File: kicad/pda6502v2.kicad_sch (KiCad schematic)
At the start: 87 parts

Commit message: kicad: schematic format version 20211123->20230121 (KiCad 7.0)
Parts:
- C1, C10, C11, C14, C15, C16, C17, C2, C22, C23, C24, C25, C26, C27, C3, C32, C4, C5, C6, C7, C8, C9: value (none) -> 0.1μF; footprint (none) -> Capacitor_SMD:C_0805_2012Metric_Pad1.18x1.45mm_HandSolder
- C12: value (none) -> 100uF; footprint (none) -> Capacitor_THT:CP_Radial_D5.0mm_P2.00mm
- C13: value (none) -> 10uF; footprint (none) -> Capacitor_THT:CP_Radial_D5.0mm_P2.00mm
- C18, C19: value (none) -> 10nF; footprint (none) -> Capacitor_SMD:C_0805_2012Metric_Pad1.18x1.45mm_HandSolder
- C20, C21: value (none) -> 10uF; footprint (none) -> Capacitor_SMD:C_0805_2012Metric_Pad1.18x1.45mm_HandSolder
- C28, C31: value (none) -> 1800 pf; footprint (none) -> Capacitor_SMD:C_0805_2012Metric_Pad1.18x1.45mm_HandSolder
- C29, C30: value (none) -> 10uF; footprint (none) -> Capacitor_Tantalum_SMD:CP_EIA-3528-15_AVX-H_Pad1.50x2.35mm_HandSolder
- D1: value (none) -> 1N5819; footprint (none) -> Diode_THT:D_DO-41_SOD81_P10.16mm_Horizontal
- D10, D3, D4, D5, D6, D7, D8, D9: value (none) -> LED; footprint (none) -> LED_SMD:LED_0805_2012Metric_Pad1.15x1.40mm_HandSolder
- D11: value (none) -> 1N4148W; footprint (none) -> Diode_SMD:D_SOD-123
- D2: value (none) -> LED; footprint (none) -> LED_THT:LED_D3.0mm
- J1: value (none) -> GPIO1; footprint (none) -> Connector_PinHeader_2.54mm:PinHeader_2x12_P2.54mm_Vertical
- J2: value (none) -> GPIO2; footprint (none) -> Connector_PinHeader_2.54mm:PinHeader_2x12_P2.54mm_Vertical
- J3: value (none) -> UART; footprint (none) -> Connector_PinHeader_2.54mm:PinHeader_2x06_P2.54mm_Vertical
- J4: value (none) -> Screw_Terminal_01x02; footprint (none) -> TerminalBlock_Phoenix:TerminalBlock_Phoenix_MPT-0,5-2-2.54_1x02_P2.54mm_Horizontal
- J5: value (none) -> Conn_02x04_Odd_Even; footprint (none) -> Connector_PinHeader_2.54mm:PinHeader_2x04_P2.54mm_Vertical
- J6: value (none) -> ICSP; footprint (none) -> Connector_PinHeader_2.54mm:PinHeader_2x03_P2.54mm_Vertical
- J7: value (none) -> SPI; footprint (none) -> Connector_PinHeader_2.54mm:PinHeader_2x10_P2.54mm_Vertical
- J8: value (none) -> FPGA_EXT; footprint (none) -> Connector_PinHeader_2.54mm:PinHeader_2x08_P2.54mm_Vertical
- J9: value (none) -> SID; footprint (none) -> Connector_PinHeader_2.54mm:PinHeader_2x04_P2.54mm_Vertical
- R1, R2, R21, R22, R23, R3, R4: value (none) -> 10K; footprint (none) -> Resistor_SMD:R_0805_2012Metric_Pad1.20x1.40mm_HandSolder
- R24: value (none) -> 255k; footprint (none) -> Resistor_SMD:R_0805_2012Metric_Pad1.20x1.40mm_HandSolder
- R25: value (none) -> 243k; footprint (none) -> Resistor_SMD:R_0805_2012Metric_Pad1.20x1.40mm_HandSolder
- R26: value (none) -> 0; footprint (none) -> Resistor_SMD:R_0805_2012Metric_Pad1.20x1.40mm_HandSolder
- R27: value (none) -> open; footprint (none) -> Resistor_SMD:R_0805_2012Metric_Pad1.20x1.40mm_HandSolder
- R28: value (none) -> 1K; footprint (none) -> Resistor_SMD:R_0805_2012Metric_Pad1.20x1.40mm_HandSolder
- R29, R30, R31, R32, R33, R34, R35, R36: value (none) -> 330; footprint (none) -> Resistor_SMD:R_0805_2012Metric_Pad1.20x1.40mm_HandSolder
- SW1: value (none) -> SW_Push; footprint (none) -> Button_Switch_THT:SW_PUSH_6mm_H5mm
- SW2: value (none) -> SW_Push; footprint (none) -> Connector_PinHeader_2.54mm:PinHeader_1x02_P2.54mm_Vertical
- U1: value (none) -> W65C02SxP; footprint (none) -> Package_DIP:DIP-40_W15.24mm
- U10: value (none) -> LT3030; footprint (none) -> Package_SO:HTSSOP-20-1EP_4.4x6.5mm_P0.65mm_EP2.85x4mm
- U11: value (none) -> SC28L92A1B; footprint (none) -> Package_QFP:PQFP-44_10x10mm_P0.8mm
- U2, U3: value (none) -> W65C22SxP; footprint (none) -> Package_DIP:DIP-40_W15.24mm
- U4: value (none) -> DS1818; footprint (none) -> Package_TO_SOT_SMD:SOT-23_Handsoldering
- U5: value (none) -> AS6C4008-55PCN; footprint (none) -> Package_DIP:DIP-32_W15.24mm
- U6: value (none) -> ARMSID; footprint (none) -> Package_DIP:DIP-28_W15.24mm_Socket
- U7: value (none) -> AT25M01; footprint (none) -> Package_SO:SOIC-8_3.9x4.9mm_P1.27mm
- U8: value (none) -> ICE40HX4K-TQ144; footprint (none) -> Package_QFP:TQFP-144_20x20mm_P0.5mm
- U9: value (none) -> TLV1117-33; footprint (none) -> Package_TO_SOT_SMD:SOT-223
- X1: value (none) -> 8 MHz; footprint (none) -> pda6502v2:Oscillator_SMD_5.0x3.2mm_HandSolder
- X2: value (none) -> 3.6864 MHz; footprint (none) -> pda6502v2:Oscillator_SMD_5.0x3.2mm_HandSolder

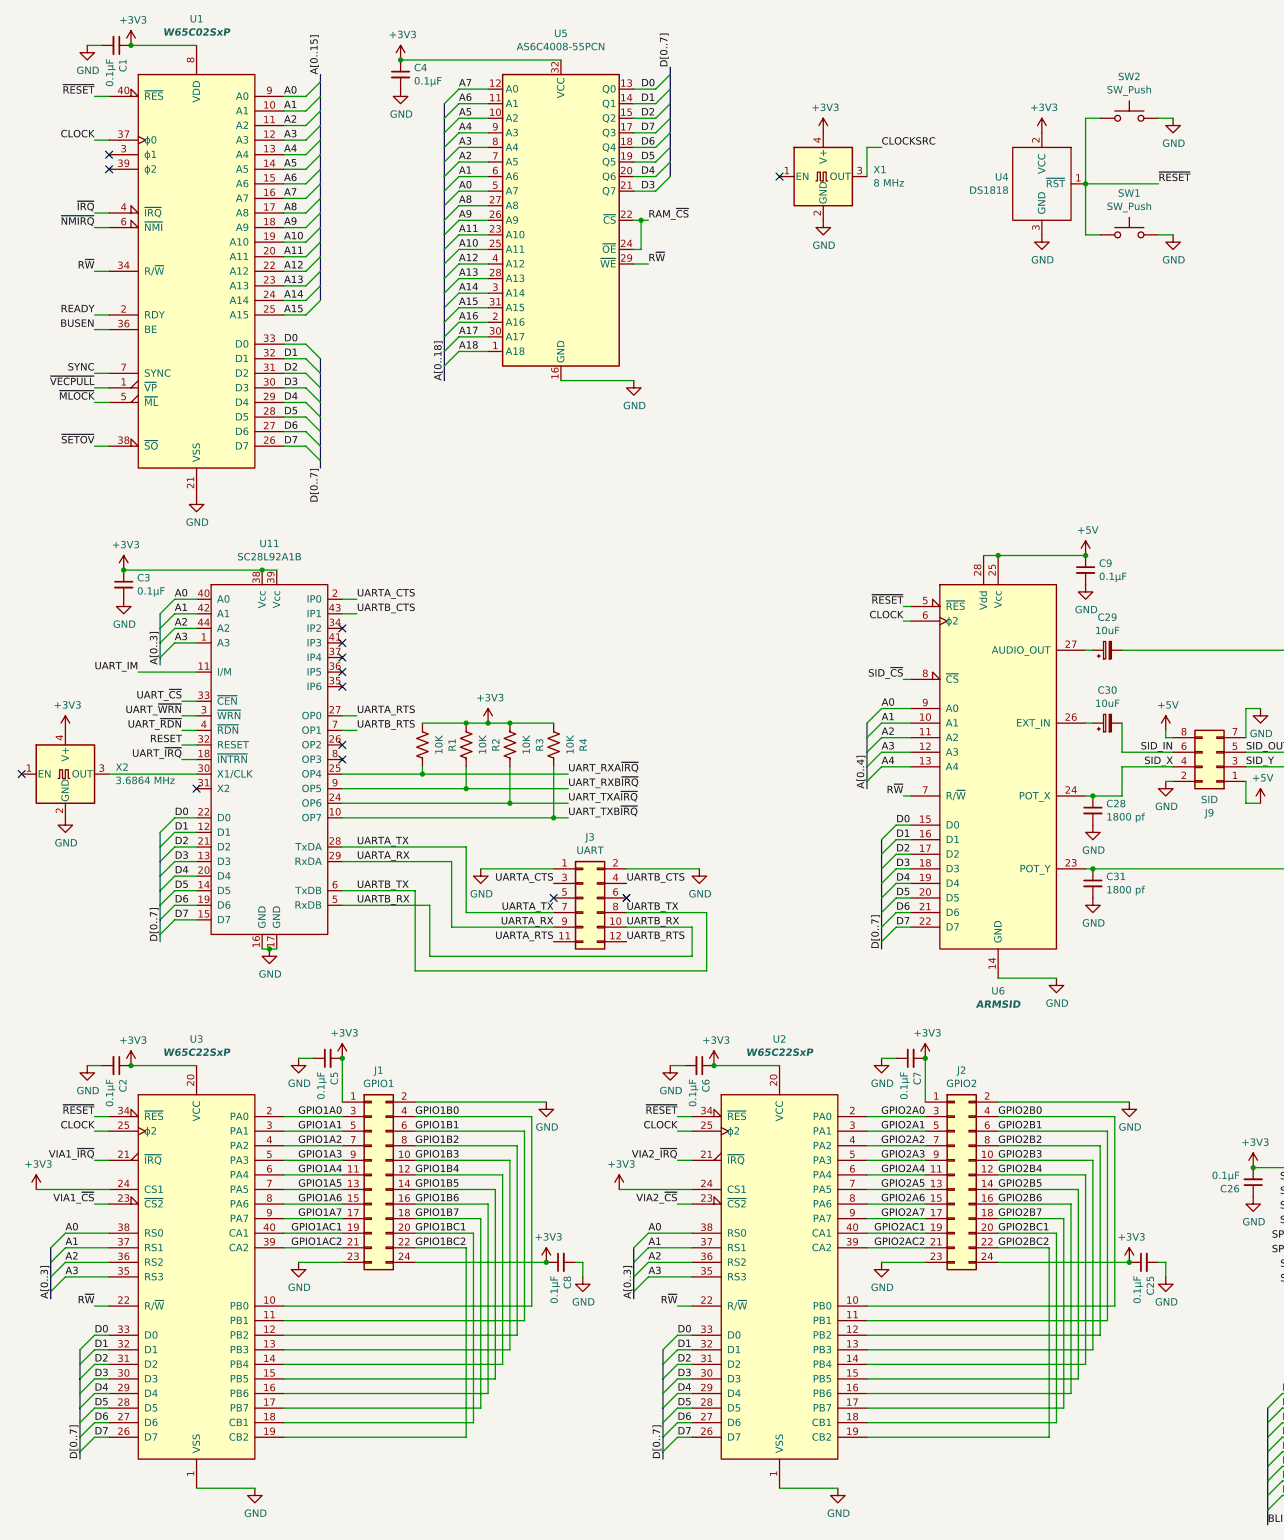
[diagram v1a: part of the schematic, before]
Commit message: kicad: schematic Electrical Rules Checker fixes
Use updated 6502-kicad-library symbols, including their 6522 instead of
our own. The symbol size/pins etc moved around, schematic adjusted.

Use new built-in capacitor symbols instead of rescued olf CP-Device.
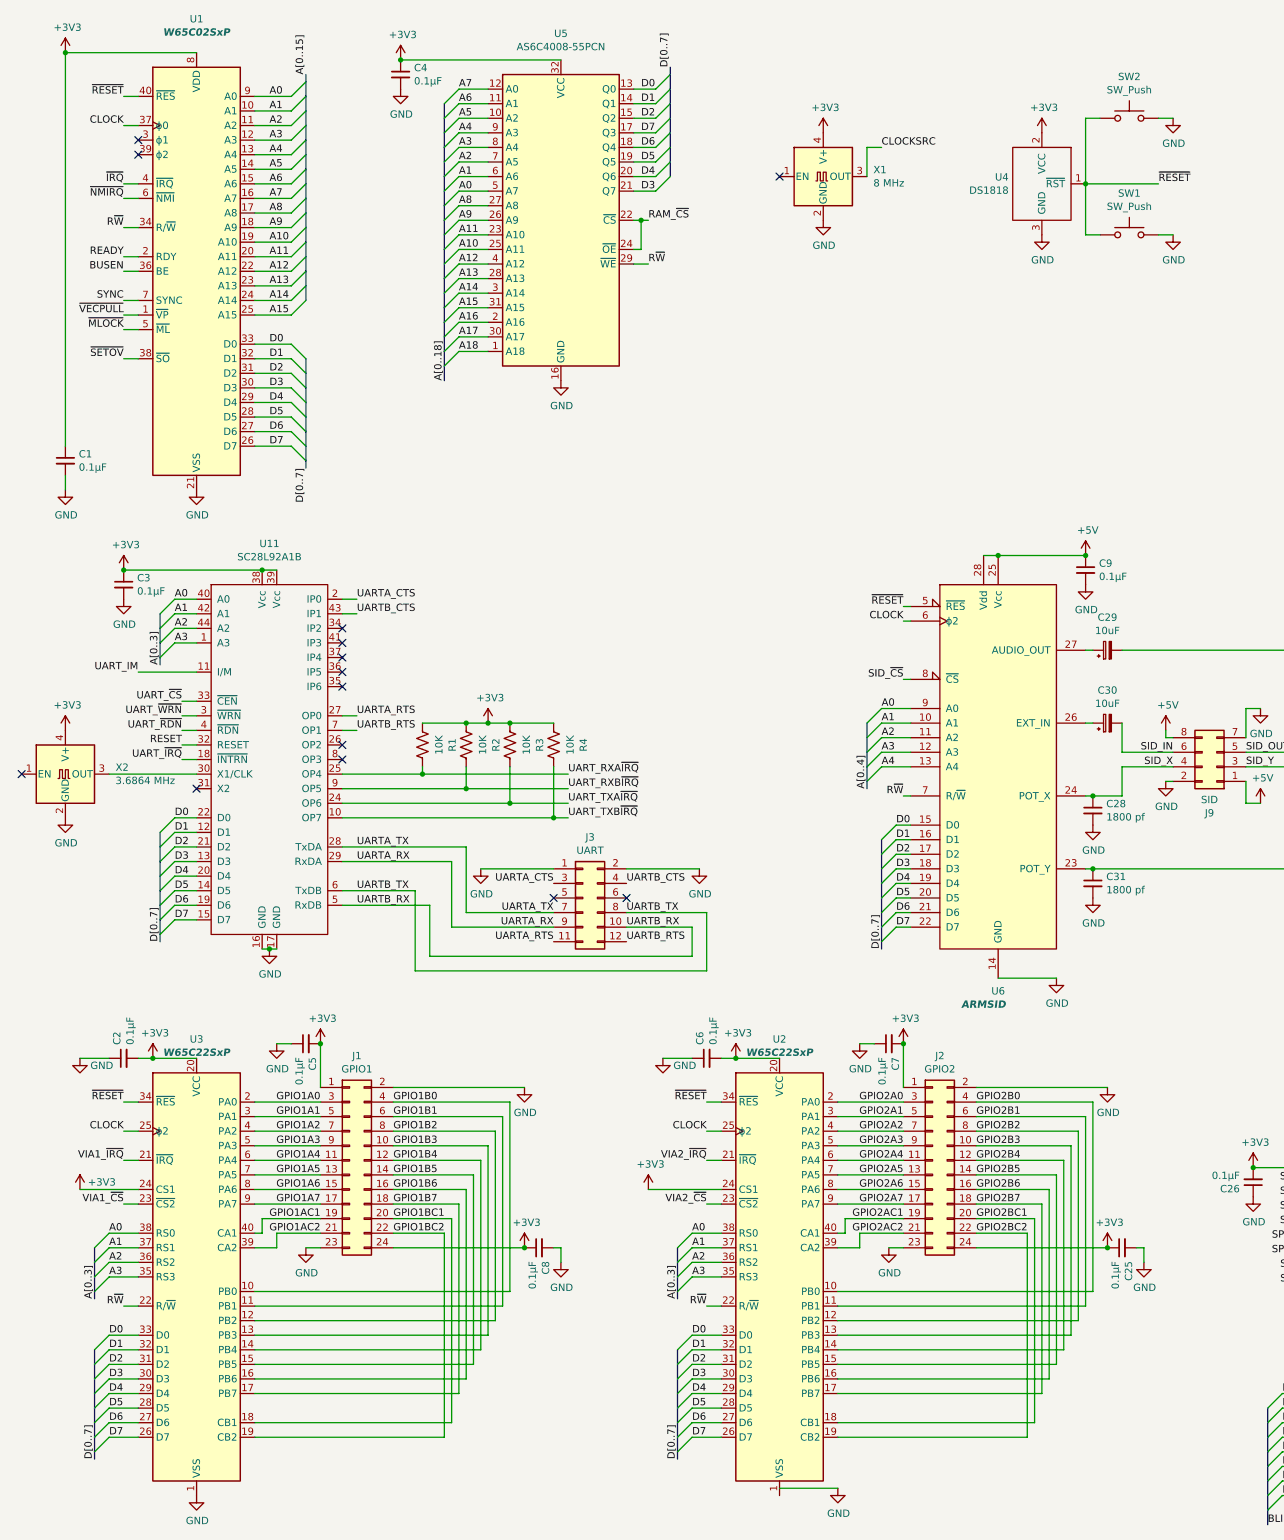
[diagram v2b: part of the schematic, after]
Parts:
- C12, C13: symbol pda6502v2-rescue:CP-Device -> Device:C_Polarized
- C29, C30: symbol pda6502v2-rescue:CP_Small-Device -> Device:C_Polarized_Small
- U1: symbol pda6502v2-rescue:W65C02SxP-65xx -> 65xx:W65C02SxP
- U2, U3: symbol pda6502v2:W65C22SxP -> 65xx:W65C22SxP
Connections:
- net +3V3: now also C2.2, C6.2; no longer C2.1, C6.1
- net GND: now also C2.1, C6.1; no longer C2.2, C6.2, U2.1 (VSS)
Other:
- moved on the sheet: C1, C2, C25, C5, C7, C8, J1, J2

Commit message: kicad: more schematic Electrical Rules Checker fixes
Updated symbols from pda6502v2 library; I think these updates were
no-ops, the library symbols hadn't really changed, but had been migrated
from older KiCad?

Also a no-op Diode updated.
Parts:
- X1, X2: footprint pda6502v2:Oscillator_SMD_5.0x3.2mm_HandSolder -> Oscillator:Oscillator_SMD_EuroQuartz_XO53-4Pin_5.0x3.2mm
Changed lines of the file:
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@@
     )
   )
-  (symbol (lib_id "pda6502v2:XO53") (at 157.48 43.18 0) (unit 1)
+  (symbol (lib_name "XO53_1") (lib_id "pda6502v2:XO53") (at 157.48 43.18 0) (unit 1)
     (in_bom yes) (on_board yes) (dnp no)
     (property "Reference" "X1" (at 166.2176 42.0116 0)
@@
       (effects (font (size 1.27 1.27)) (justify left))
     )
-    (property "Footprint" "pda6502v2:Oscillator_SMD_5.0x3.2mm_HandSolder" (at 175.26 52.07 0)
+    (property "Footprint" "Oscillator:Oscillator_SMD_EuroQuartz_XO53-4Pin_5.0x3.2mm" (at 175.26 52.07 0)
       (effects (font (size 1.27 1.27)) hide)
     )
@@
       (effects (font (size 1.27 1.27)) (justify left))
     )
-    (property "Footprint" "pda6502v2:Oscillator_SMD_5.0x3.2mm_HandSolder" (at 43.18 156.21 0)
+    (property "Footprint" "Oscillator:Oscillator_SMD_EuroQuartz_XO53-4Pin_5.0x3.2mm" (at 43.18 156.21 0)
       (effects (font (size 1.27 1.27)) hide)
     )
@@
       (effects (font (size 1.27 1.27)) hide)
     )
+    (property "Sim.Device" "D" (at 292.1 199.39 0)
+      (effects (font (size 1.27 1.27)) hide)
+    )
+    (property "Sim.Pins" "1=K 2=A" (at 292.1 199.39 0)
+      (effects (font (size 1.27 1.27)) hide)
+    )
